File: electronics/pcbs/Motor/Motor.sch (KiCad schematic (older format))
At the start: 13 parts, among them J1 Left Encoder, J2 Right Encoder, J3 I2C Bus, P1 Power, P2 Analog, P3 Digital, P4 Digital, P5 CONN_01X01, P6 CONN_01X01, P7 CONN_01X01, P8 CONN_01X01, U1 Left Nano, U2 Right Nano

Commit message: Motor PCB: Created a footprint for the Arduino Nano. Assigned footprints to the components on the Motor schematic.
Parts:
- J1, J2, J3: footprint (none) -> Connectors_Samtec:SL-104-X-XX_1x04
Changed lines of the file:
@@
 F 0 "J3" H 6350 1800 50  0000 C CNN
 F 1 "I2C Bus" H 6350 1300 50  0000 C CNN
-F 2 "" H 6350 1600 50  0001 C CNN
+F 2 "Connectors_Samtec:SL-104-X-XX_1x04" H 6350 1600 50  0001 C CNN
 F 3 "" H 6350 1600 50  0001 C CNN
 	1    6350 1600
@@
 F 0 "J1" H 5150 3700 50  0000 C CNN
 F 1 "Left Encoder" H 5250 3200 50  0000 C CNN
-F 2 "" H 5150 3500 50  0001 C CNN
+F 2 "Connectors_Samtec:SL-104-X-XX_1x04" H 5150 3500 50  0001 C CNN
 F 3 "" H 5150 3500 50  0001 C CNN
 	1    5150 3500
@@
 F 0 "J2" H 6350 3700 50  0000 C CNN
 F 1 "Right Encoder" H 6450 3200 50  0000 C CNN
-F 2 "" H 6350 3500 50  0001 C CNN
+F 2 "Connectors_Samtec:SL-104-X-XX_1x04" H 6350 3500 50  0001 C CNN
 F 3 "" H 6350 3500 50  0001 C CNN
 	1    6350 3500

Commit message: Motor PCB: First draft of PCB.
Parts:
- U1, U2: footprint (none) -> Arduino_Nano:Arduino_Nano
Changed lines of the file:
@@
 F 0 "U1" H 2150 1700 60  0000 C CNN
 F 1 "Left Nano" H 2150 1600 60  0000 C CNN
-F 2 "" H 1400 500 60  0001 C CNN
+F 2 "Arduino_Nano:Arduino_Nano" H 1400 500 60  0001 C CNN
 F 3 "" H 1400 500 60  0001 C CNN
 	1    2150 1500
@@
 F 0 "U1" H 1950 2800 60  0000 C CNN
 F 1 "Left Nano" H 1950 2700 60  0000 C CNN
-F 2 "" H 1200 1600 60  0001 C CNN
+F 2 "Arduino_Nano:Arduino_Nano" H 1200 1600 60  0001 C CNN
 F 3 "" H 1200 1600 60  0001 C CNN
 	2    1950 2600
@@
 F 0 "U1" H 2000 4550 60  0000 C CNN
 F 1 "Left Nano" H 2000 4450 60  0000 C CNN
-F 2 "" H 1250 3350 60  0001 C CNN
+F 2 "Arduino_Nano:Arduino_Nano" H 1250 3350 60  0001 C CNN
 F 3 "" H 1250 3350 60  0001 C CNN
 	3    2000 4350
@@
 F 0 "U2" H 3950 1700 60  0000 C CNN
 F 1 "Right Nano" H 3950 1600 60  0000 C CNN
-F 2 "" H 3200 500 60  0001 C CNN
+F 2 "Arduino_Nano:Arduino_Nano" H 3200 500 60  0001 C CNN
 F 3 "" H 3200 500 60  0001 C CNN
 	1    3950 1500
@@
 F 0 "U2" H 3750 2800 60  0000 C CNN
 F 1 "Right Nano" H 3750 2700 60  0000 C CNN
-F 2 "" H 3000 1600 60  0001 C CNN
+F 2 "Arduino_Nano:Arduino_Nano" H 3000 1600 60  0001 C CNN
 F 3 "" H 3000 1600 60  0001 C CNN
 	2    3750 2600
@@
 F 0 "U2" H 3800 4550 60  0000 C CNN
 F 1 "Right Nano" H 3800 4450 60  0000 C CNN
-F 2 "" H 3050 3350 60  0001 C CNN
+F 2 "Arduino_Nano:Arduino_Nano" H 3050 3350 60  0001 C CNN
 F 3 "" H 3050 3350 60  0001 C CNN
 	3    3800 4350

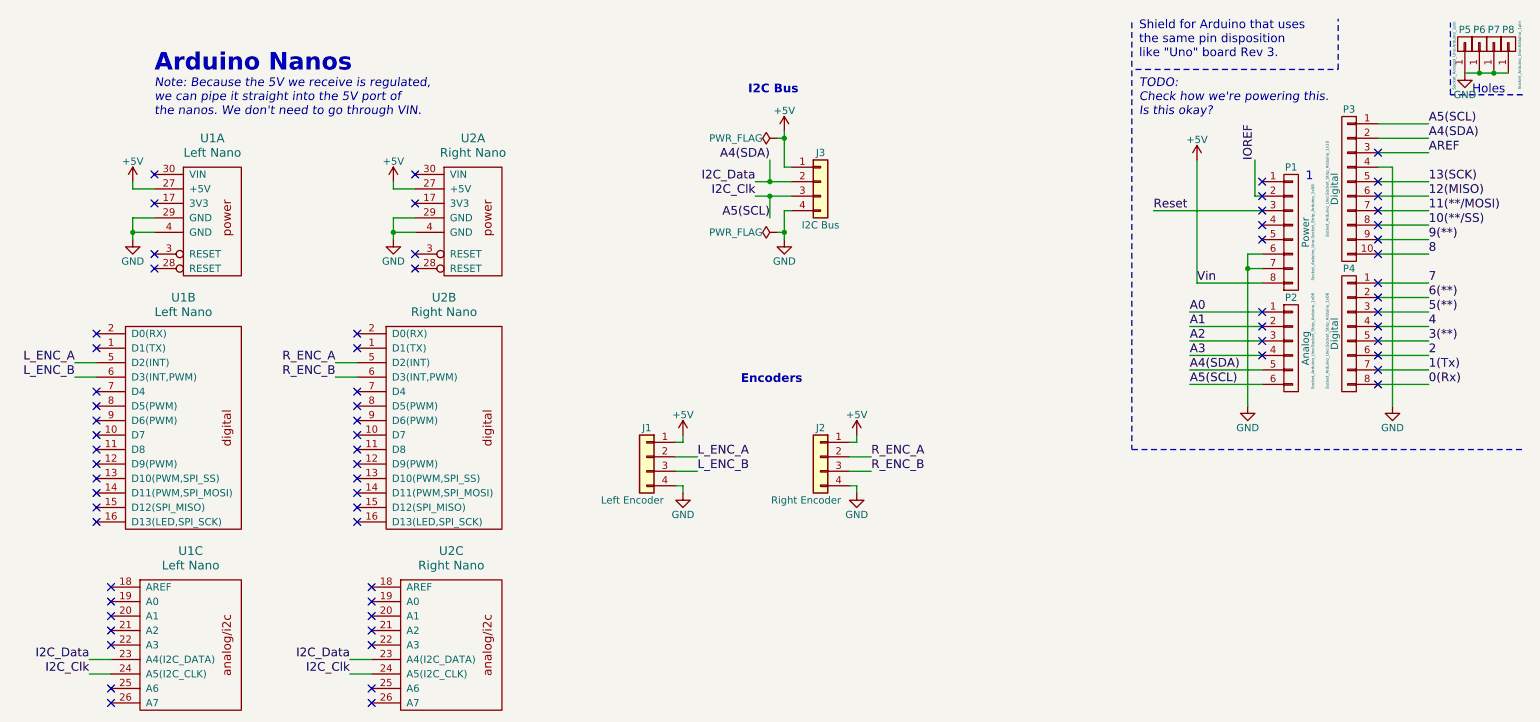
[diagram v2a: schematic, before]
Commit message: Motor PCB: Uno is now powered by BATT+; added screw terminal for battery input.
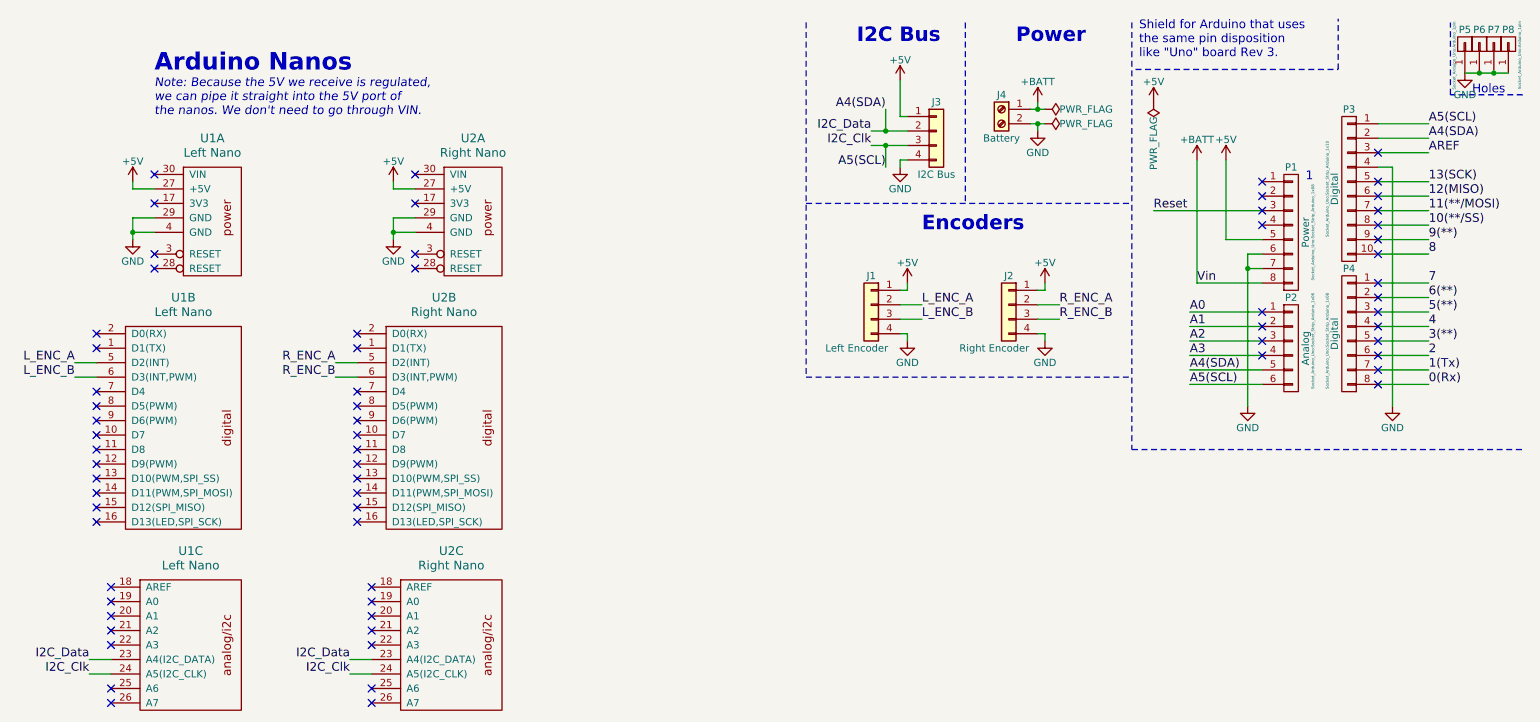
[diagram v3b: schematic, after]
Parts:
- added J4: Battery, Connectors_Terminal_Blocks:TerminalBlock_bornier-2_P5.08mm, symbol Screw_Terminal_01x02
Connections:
- net +5V: now also P1.5 (P5); no longer P1.8 (P8)
- net GND: now also J4.2 (Pin_2)
- net IOREF: no longer names the net of P1.2 (P2)
- new net +BATT: J4.1 (Pin_1), P1.8 (P8)
- no-connect marks 70 -> 69
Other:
- note added: "Power"
- note removed: "TODO:\nCheck how we're powering this.\nIs this okay?"
- moved on the sheet: J1, J2, J3
